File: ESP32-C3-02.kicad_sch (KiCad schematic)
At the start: 5 parts, among them J3 GSD090012SEU, U3 ESP32-C3-WROOM-02-H4, U4 CP2102N-Axx-xQFN20, U5 USBLC6-2SC6, U6 W25Q32JVSSIQ

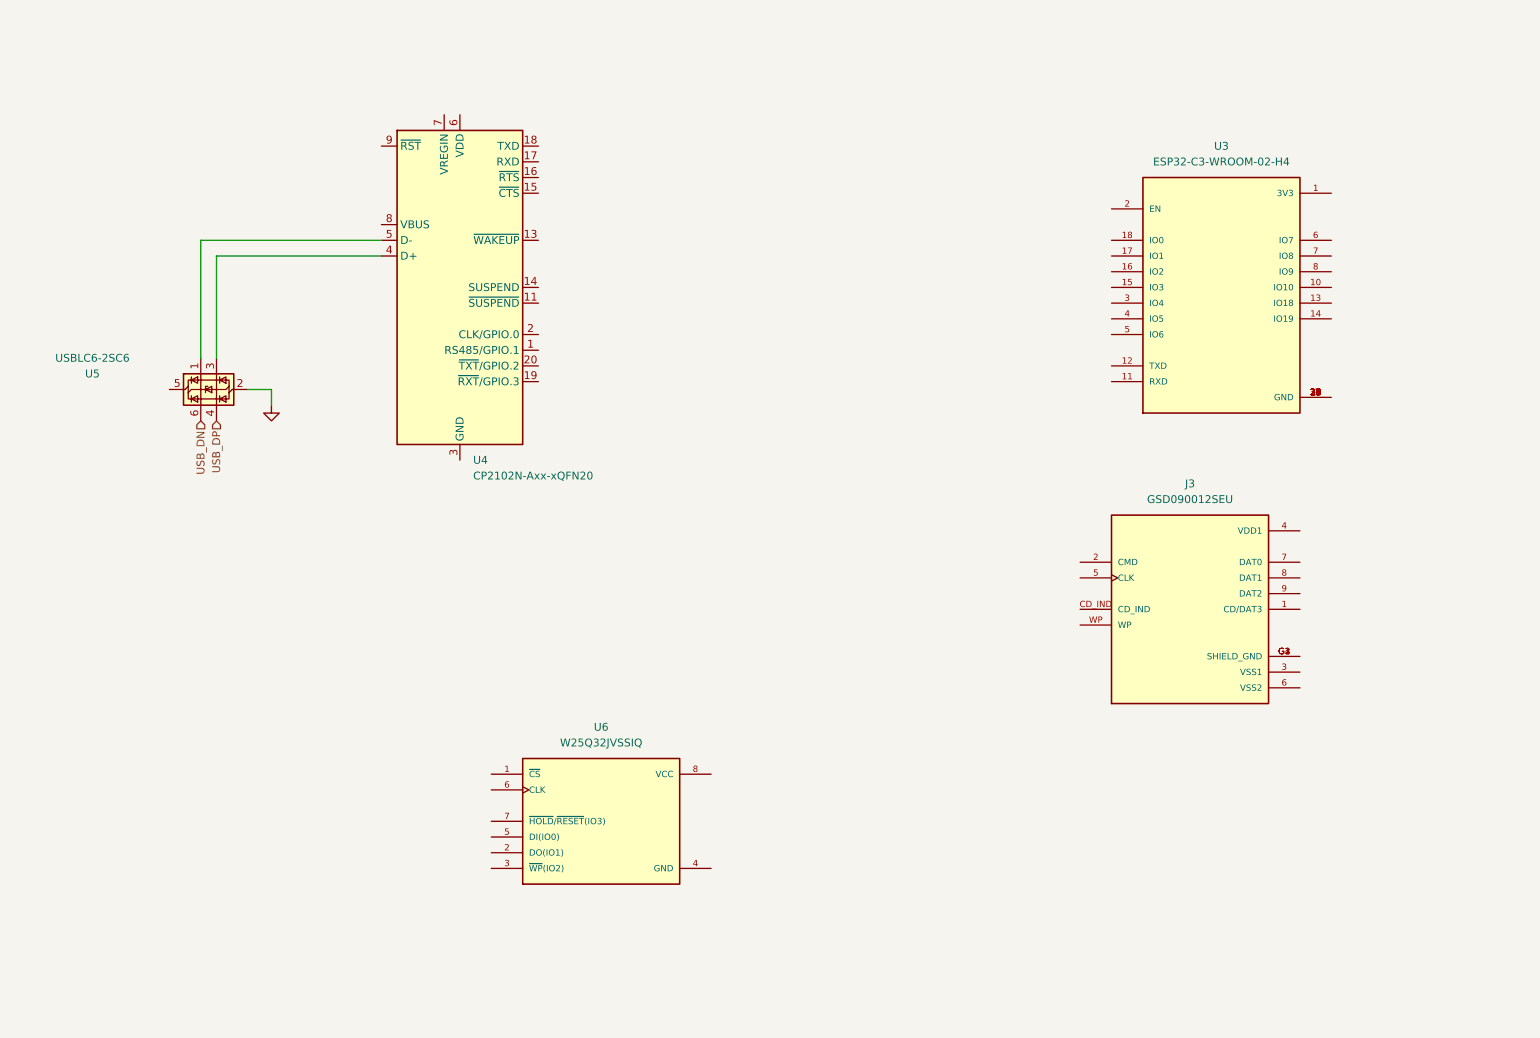
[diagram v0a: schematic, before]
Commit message: More of the Page of ESP32
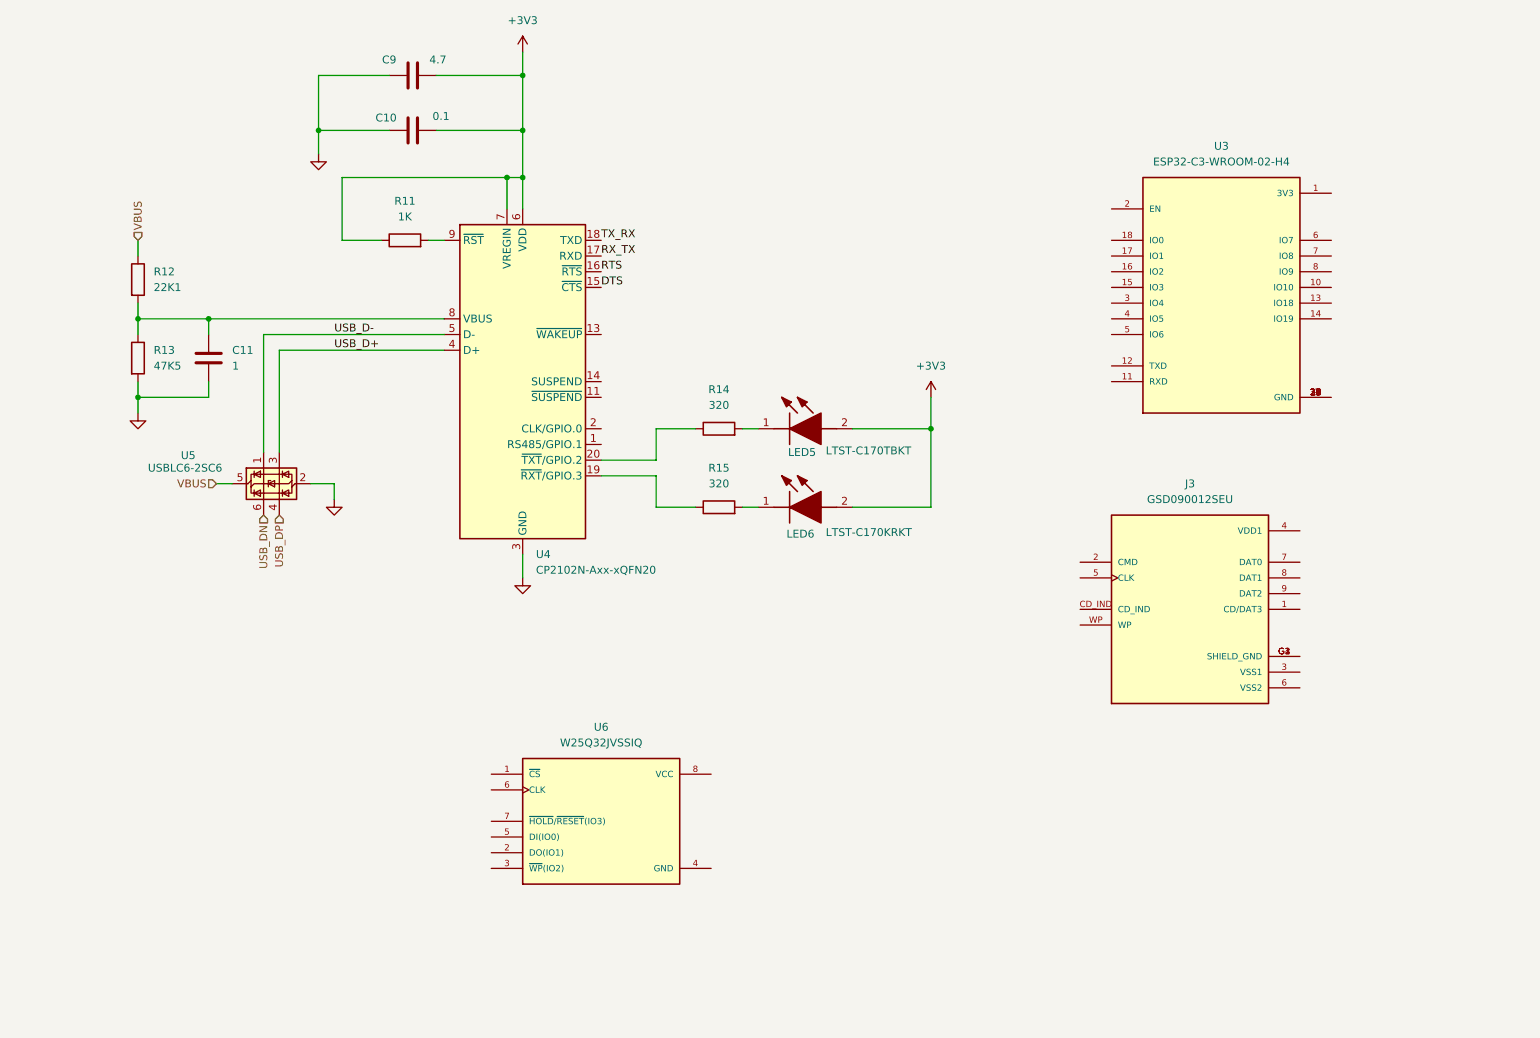
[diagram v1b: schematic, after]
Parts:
- added C10: 0.1, symbol Device:C
- added C11: 1, symbol Device:C
- added C9: 4.7, symbol Device:C
- added LED5: LTST-C170TBKT, LEDC2012X120N, symbol LTST-C170TBKT:LTST-C170TBKT
- added LED6: LTST-C170KRKT, LEDC2012X120N, symbol LTST-C170KRKT:LTST-C170KRKT
- added R11: 1K, symbol Device:R
- added R12: 22K1, symbol Device:R
- added R13: 47K5, symbol Device:R
- added R14, R15: 320, symbol Device:R
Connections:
- net GND: now also U4.12 (GND), U4.21 (GND), U4.3 (GND), C10.1, C11.2, C9.1, R13.2
- net DTS: now reaches U4.15 (~{CTS})
- net RTS: now reaches U4.16 (~{RTS})
- net RX_TX: now reaches U4.17 (RXD)
- net TX_RX: now reaches U4.18 (TXD)
- net at U4.19 (~{RXT}/GPIO.3): now also R15.1
- net at U4.20 (~{TXT}/GPIO.2): now also R14.1
- net USB_D+: now reaches U4.4 (D+), U5.3 (I/O2)
- net USB_D-: now reaches U4.5 (D-), U5.1 (I/O1)
- net +3V3: now reaches U4.6 (VDD)
- net +3V3: now also U4.7 (VREGIN), C10.2, C9.2, LED5.2 (A), LED6.2 (A), R11.1
- net at U4.8 (VBUS): now also C11.1, R12.2, R13.1
- net at U4.9 (~{RST}): now also R11.2
- net VBUS: now reaches U5.5 (VBUS)
- net VBUS: now also R12.1
- new net: LED6.1 (K), R15.2
- new net: LED5.1 (K), R14.2
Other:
- moved on the sheet: U4, U5

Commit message: Update ESP32-C3-02.kicad_sch
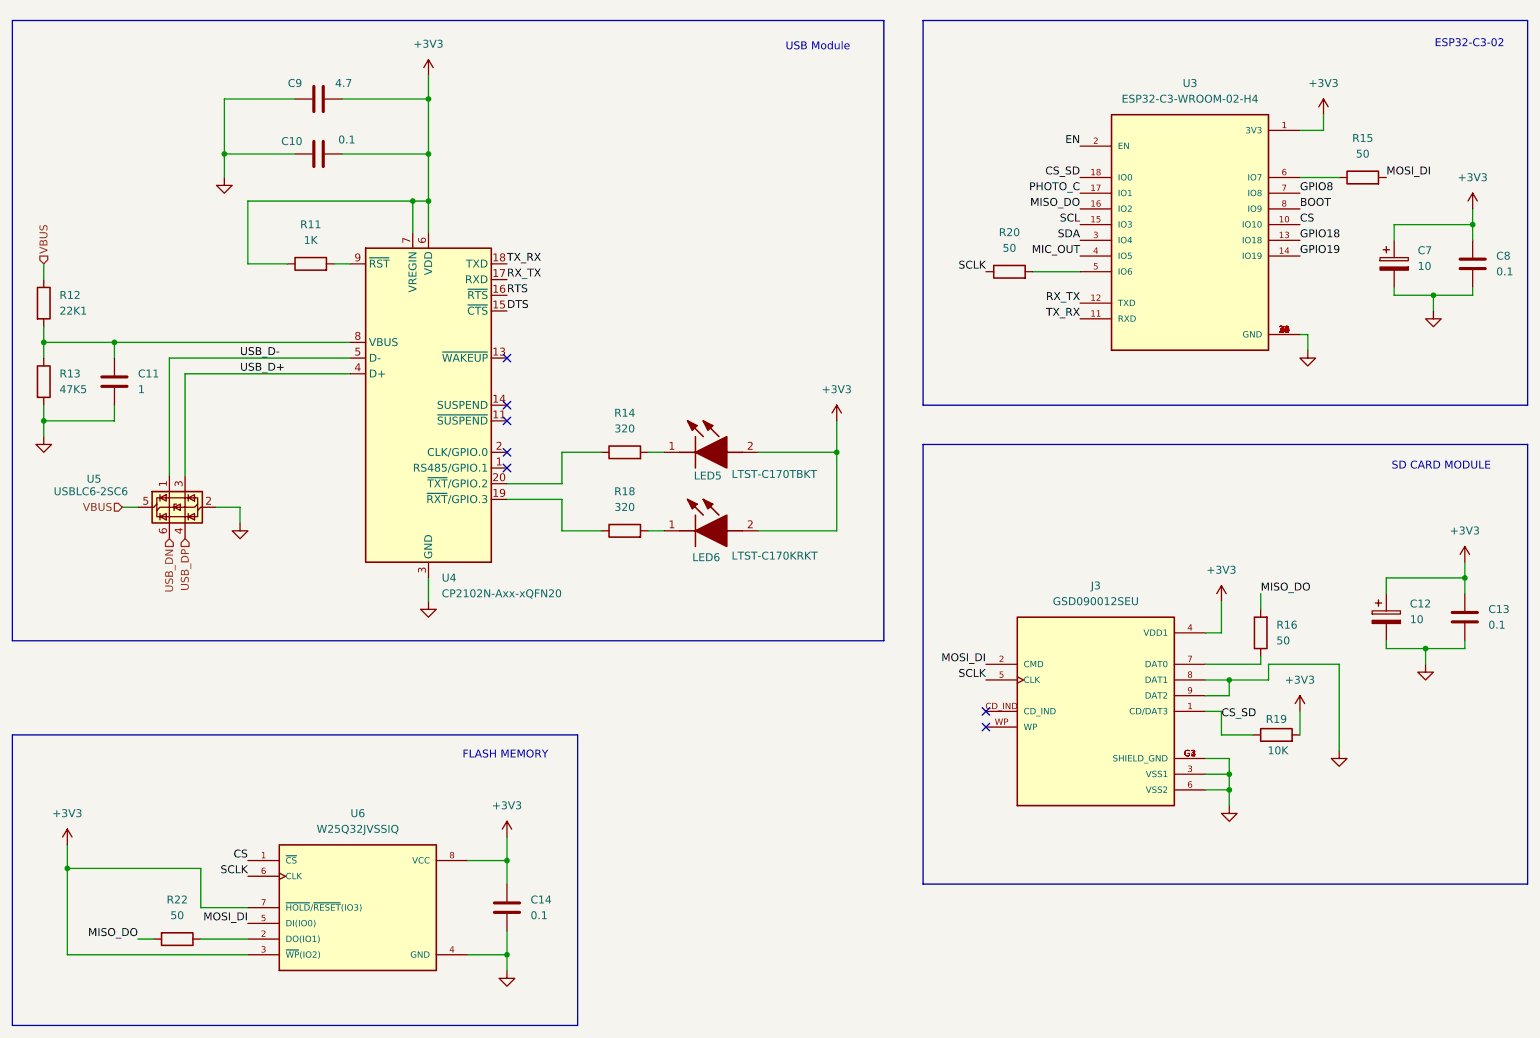
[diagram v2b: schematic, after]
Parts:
- added C12, C7: 10, symbol Device:C_Polarized
- added C13, C14, C8: 0.1, symbol Device:C
- added R15, R16, R20, R22: 50, symbol Device:R
- added R19: 10K, symbol Device:R
- renumbered R15 to R18
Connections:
- net +3V3: now also J3.4 (VDD1), U3.1 (3V3), U6.3 (~{WP}(IO2)), U6.7 (~{HOLD}/~{RESET}(IO3)), U6.8 (VCC), C12.1, C13.1, C14.1, C7.1, C8.1, R19.2
- net GND: now also J3.3 (VSS1), J3.6 (VSS2), J3.8 (DAT1), J3.9 (DAT2), J3.G1 (SHIELD_GND), J3.G2 (SHIELD_GND), J3.G3 (SHIELD_GND), J3.G4 (SHIELD_GND), U3.19 (GND), U3.20 (GND), U3.21 (GND), U3.22 (GND), U3.23 (GND), U3.24 (GND), U3.25 (GND), U3.26 (GND), U3.27 (GND), U3.28 (GND), U3.29 (GND), U3.30 (GND), U3.31 (GND), U3.32 (GND), U3.33 (GND), U3.34 (GND), U3.35 (GND), U3.36 (GND), U3.37 (GND), U3.38 (GND), U3.39 (GND), U3.9 (GND), U6.4 (GND), C12.2, C13.2, C14.2, C7.2, C8.2
- net RX_TX: now also U3.12 (TXD)
- net TX_RX: now also U3.11 (RXD)
- net CS: now reaches U3.10 (IO10)
- net CS: now also U6.1 (~{CS})
- net GPIO18: now reaches U3.13 (IO18)
- net GPIO19: now reaches U3.14 (IO19)
- net SCL: now reaches U3.15 (IO3)
- net MISO_DO: now reaches U3.16 (IO2)
- net MISO_DO: now also R16.2, R22.2
- net PHOTO_C: now reaches U3.17 (IO1)
- net CS_SD: now reaches U3.18 (IO0)
- net CS_SD: now also J3.1 (CD/DAT3), R19.1
- net EN: now reaches U3.2 (EN)
- net SDA: now reaches U3.3 (IO4)
- net MIC_OUT: now reaches U3.4 (IO5)
- net at U3.5 (IO6): now also R20.2
- net at U3.6 (IO7): now also R15.1
- net GPIO8: now reaches U3.7 (IO8)
- net BOOT: now reaches U3.8 (IO9)
- net at U6.2 (DO(IO1)): now also R22.1
- net MOSI_DI: now reaches U6.5 (DI(IO0))
- net MOSI_DI: now also J3.2 (CMD), R15.2
- net SCLK: now reaches U6.6 (CLK)
- net SCLK: now also J3.5 (CLK), R20.1
- net at J3.7 (DAT0): now also R16.1
- no-connect marks 0 -> 7
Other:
- note added: "ESP32-C3-02"
- note added: "FLASH MEMORY"
- note added: "SD CARD MODULE"
- note added: "USB Module"
- moved on the sheet: C10, C11, C9, J3, LED5, LED6, R11, R12, R13, R14, R18, U3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
